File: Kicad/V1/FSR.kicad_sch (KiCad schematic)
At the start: 3 parts

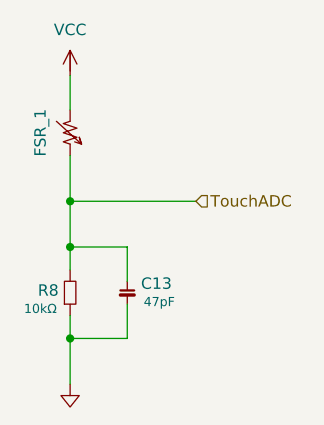
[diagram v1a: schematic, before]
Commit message: ERC almost done, footprint to assign
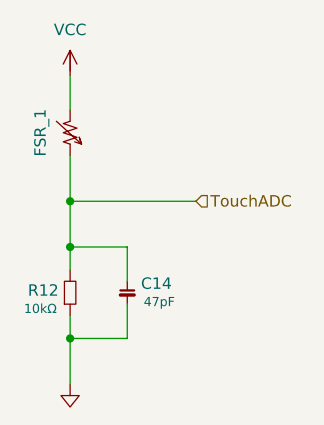
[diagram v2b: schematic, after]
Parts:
- renumbered C13 to C14, R8 to R12
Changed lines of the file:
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@@
 		(in_pos_files yes)
 		(dnp no)
-		(property "Reference" "C13"
+		(property "Reference" "C14"
 			(at 32.004 47.244 0)
 			(show_name no)
@@
 			(project "G-Love"
 				(path "/808bc5ea-49ac-4454-ba77-8b20d01ce159/7de4e8e6-4751-4acb-b71f-e492a47c8332/15052d3f-5b94-4226-97e2-3e9ab10fafda"
-					(reference "C13")
+					(reference "C14")
 					(unit 1)
 				)
 				(path "/808bc5ea-49ac-4454-ba77-8b20d01ce159/7de4e8e6-4751-4acb-b71f-e492a47c8332/32c3dc22-6eac-49d0-b512-767615f82205"
-					(reference "C14")
+					(reference "C27")
 					(unit 1)
 				)
 				(path "/808bc5ea-49ac-4454-ba77-8b20d01ce159/7de4e8e6-4751-4acb-b71f-e492a47c8332/3f48e459-1dc8-4eb9-8adc-befbe01eab22"
+					(reference "C15")
+					(unit 1)
+				)
+				(path "/808bc5ea-49ac-4454-ba77-8b20d01ce159/7de4e8e6-4751-4acb-b71f-e492a47c8332/5442b494-eff8-4ddd-bc03-bcc1bea75842"
 					(reference "C16")
-					(unit 1)
-				)
-				(path "/808bc5ea-49ac-4454-ba77-8b20d01ce159/7de4e8e6-4751-4acb-b71f-e492a47c8332/5442b494-eff8-4ddd-bc03-bcc1bea75842"
-					(reference "C15")
 					(unit 1)
 				)
@@
 		(in_pos_files yes)
 		(dnp no)
-		(property "Reference" "R8"
+		(property "Reference" "R12"
 			(at 22.86 48.006 90)
 			(show_name no)
@@
 			(project "G-Love"
 				(path "/808bc5ea-49ac-4454-ba77-8b20d01ce159/7de4e8e6-4751-4acb-b71f-e492a47c8332/15052d3f-5b94-4226-97e2-3e9ab10fafda"
-					(reference "R8")
+					(reference "R12")
 					(unit 1)
 				)
 				(path "/808bc5ea-49ac-4454-ba77-8b20d01ce159/7de4e8e6-4751-4acb-b71f-e492a47c8332/32c3dc22-6eac-49d0-b512-767615f82205"
-					(reference "R9")
+					(reference "R19")
 					(unit 1)
 				)
 				(path "/808bc5ea-49ac-4454-ba77-8b20d01ce159/7de4e8e6-4751-4acb-b71f-e492a47c8332/3f48e459-1dc8-4eb9-8adc-befbe01eab22"
-					(reference "R11")
+					(reference "R13")
 					(unit 1)
 				)
 				(path "/808bc5ea-49ac-4454-ba77-8b20d01ce159/7de4e8e6-4751-4acb-b71f-e492a47c8332/5442b494-eff8-4ddd-bc03-bcc1bea75842"
-					(reference "R10")
+					(reference "R14")
 					(unit 1)
 				)
 				(path "/808bc5ea-49ac-4454-ba77-8b20d01ce159/7de4e8e6-4751-4acb-b71f-e492a47c8332/f906f610-f118-4325-955e-6566f843376d"
-					(reference "R12")
+					(reference "R15")
 					(unit 1)
 				)
@@
 		(dnp no)
 		(fields_autoplaced yes)
-		(property "Reference" "#PWR09"
+		(property "Reference" "#PWR016"
 			(at 27.94 24.638 0)
 			(hide yes)
@@
 			(project "G-Love"
 				(path "/808bc5ea-49ac-4454-ba77-8b20d01ce159/7de4e8e6-4751-4acb-b71f-e492a47c8332/15052d3f-5b94-4226-97e2-3e9ab10fafda"
-					(reference "#PWR09")
+					(reference "#PWR016")
 					(unit 1)
 				)
 				(path "/808bc5ea-49ac-4454-ba77-8b20d01ce159/7de4e8e6-4751-4acb-b71f-e492a47c8332/32c3dc22-6eac-49d0-b512-767615f82205"
-					(reference "#PWR010")
+					(reference "#PWR027")
 					(unit 1)
 				)
 				(path "/808bc5ea-49ac-4454-ba77-8b20d01ce159/7de4e8e6-4751-4acb-b71f-e492a47c8332/3f48e459-1dc8-4eb9-8adc-befbe01eab22"
-					(reference "#PWR012")
+					(reference "#PWR017")
 					(unit 1)
 				)
 				(path "/808bc5ea-49ac-4454-ba77-8b20d01ce159/7de4e8e6-4751-4acb-b71f-e492a47c8332/5442b494-eff8-4ddd-bc03-bcc1bea75842"
-					(reference "#PWR011")
+					(reference "#PWR018")
 					(unit 1)
 				)
 				(path "/808bc5ea-49ac-4454-ba77-8b20d01ce159/7de4e8e6-4751-4acb-b71f-e492a47c8332/f906f610-f118-4325-955e-6566f843376d"
-					(reference "#PWR013")
+					(reference "#PWR019")
 					(unit 1)
 				)
@@
 				)
 				(path "/808bc5ea-49ac-4454-ba77-8b20d01ce159/7de4e8e6-4751-4acb-b71f-e492a47c8332/32c3dc22-6eac-49d0-b512-767615f82205"
+					(reference "FSR_5")
+					(unit 1)
+				)
+				(path "/808bc5ea-49ac-4454-ba77-8b20d01ce159/7de4e8e6-4751-4acb-b71f-e492a47c8332/3f48e459-1dc8-4eb9-8adc-befbe01eab22"
 					(reference "FSR_2")
-					(unit 1)
-				)
-				(path "/808bc5ea-49ac-4454-ba77-8b20d01ce159/7de4e8e6-4751-4acb-b71f-e492a47c8332/3f48e459-1dc8-4eb9-8adc-befbe01eab22"
-					(reference "FSR_4")
 					(unit 1)
 				)
@@
 				)
 				(path "/808bc5ea-49ac-4454-ba77-8b20d01ce159/7de4e8e6-4751-4acb-b71f-e492a47c8332/f906f610-f118-4325-955e-6566f843376d"
-					(reference "FSR_5")
+					(reference "FSR_4")
 					(unit 1)
 				)
@@
 		(dnp no)
 		(fields_autoplaced yes)
-		(property "Reference" "GND011"
+		(property "Reference" "GND017"
 			(at 24.13 61.976 0)
 			(hide yes)
@@
 			(project "G-Love"
 				(path "/808bc5ea-49ac-4454-ba77-8b20d01ce159/7de4e8e6-4751-4acb-b71f-e492a47c8332/15052d3f-5b94-4226-97e2-3e9ab10fafda"
-					(reference "GND011")
+					(reference "GND017")
 					(unit 1)
 				)
 				(path "/808bc5ea-49ac-4454-ba77-8b20d01ce159/7de4e8e6-4751-4acb-b71f-e492a47c8332/32c3dc22-6eac-49d0-b512-767615f82205"
-					(reference "GND012")
+					(reference "GND030")
 					(unit 1)
 				)
 				(path "/808bc5ea-49ac-4454-ba77-8b20d01ce159/7de4e8e6-4751-4acb-b71f-e492a47c8332/3f48e459-1dc8-4eb9-8adc-befbe01eab22"
-					(reference "GND014")
+					(reference "GND018")
 					(unit 1)
 				)
 				(path "/808bc5ea-49ac-4454-ba77-8b20d01ce159/7de4e8e6-4751-4acb-b71f-e492a47c8332/5442b494-eff8-4ddd-bc03-bcc1bea75842"
-					(reference "GND013")
+					(reference "GND019")
 					(unit 1)
 				)
 				(path "/808bc5ea-49ac-4454-ba77-8b20d01ce159/7de4e8e6-4751-4acb-b71f-e492a47c8332/f906f610-f118-4325-955e-6566f843376d"
-					(reference "GND015")
-					(unit 1)
-				)
+					(reference "GND020")
+					(unit 1)
+				)

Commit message: ERC Check
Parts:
- FSR_1: footprint MyGlove:PinHeader_1x02_Pas2.54mm_ -> MyGlove:PinHeader_1x02_P2.54mm_Vertical
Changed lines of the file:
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@@
 			)
 		)
-		(property "Footprint" "MyGlove:PinHeader_1x02_Pas2.54mm_"
+		(property "Footprint" "MyGlove:PinHeader_1x02_P2.54mm_Vertical"
 			(at 24.13 30.48 0)
 			(hide yes)

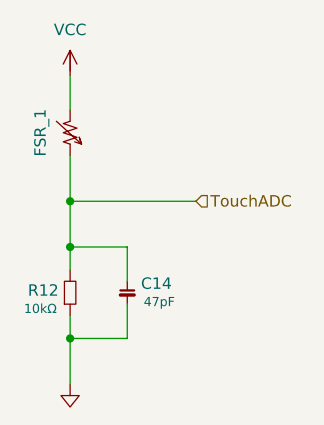
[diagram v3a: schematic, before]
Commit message: correction 328p et ajout d'un capa
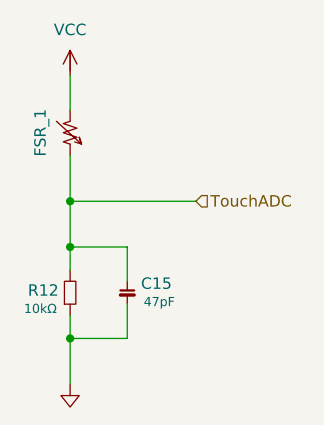
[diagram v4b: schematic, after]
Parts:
- renumbered C14 to C15
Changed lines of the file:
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@@
 		(in_pos_files yes)
 		(dnp no)
-		(property "Reference" "C14"
+		(property "Reference" "C15"
 			(at 32.004 47.244 0)
 			(show_name no)
@@
 			(project "G-Love"
 				(path "/808bc5ea-49ac-4454-ba77-8b20d01ce159/7de4e8e6-4751-4acb-b71f-e492a47c8332/15052d3f-5b94-4226-97e2-3e9ab10fafda"
-					(reference "C14")
+					(reference "C15")
 					(unit 1)
 				)
 				(path "/808bc5ea-49ac-4454-ba77-8b20d01ce159/7de4e8e6-4751-4acb-b71f-e492a47c8332/32c3dc22-6eac-49d0-b512-767615f82205"
-					(reference "C27")
+					(reference "C28")
 					(unit 1)
 				)
 				(path "/808bc5ea-49ac-4454-ba77-8b20d01ce159/7de4e8e6-4751-4acb-b71f-e492a47c8332/3f48e459-1dc8-4eb9-8adc-befbe01eab22"
-					(reference "C15")
+					(reference "C16")
 					(unit 1)
 				)
 				(path "/808bc5ea-49ac-4454-ba77-8b20d01ce159/7de4e8e6-4751-4acb-b71f-e492a47c8332/5442b494-eff8-4ddd-bc03-bcc1bea75842"
-					(reference "C16")
+					(reference "C17")
 					(unit 1)
 				)
 				(path "/808bc5ea-49ac-4454-ba77-8b20d01ce159/7de4e8e6-4751-4acb-b71f-e492a47c8332/f906f610-f118-4325-955e-6566f843376d"
-					(reference "C17")
+					(reference "C18")
 					(unit 1)
 				)
